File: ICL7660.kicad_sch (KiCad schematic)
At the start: 14 parts, among them J1 Vin, J2 GND, J3 Vout, J4 GND, J5 -Vout, U1 ICL7660

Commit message: 配置を修正
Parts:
- removed J4: GND, Connector_PinHeader_2.54mm:PinHeader_1x01_P2.54mm_Vertical, symbol Connector:Conn_01x01_Pin
- added H1, H2: MountingHole, MountingHole:MountingHole_3.2mm_M3, symbol Mechanical:MountingHole
- C1, C5: footprint Capacitor_THT:CP_Radial_D6.3mm_P2.50mm -> Capacitor_THT:CP_Radial_D10.0mm_P2.50mm
- R1, R2: footprint Resistor_THT:R_Axial_DIN0204_L3.6mm_D1.6mm_P7.62mm_Horizontal -> Resistor_THT:R_Axial_DIN0204_L3.6mm_D1.6mm_P2.54mm_Vertical
- renumbered J5 to J4
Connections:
- net GND: now also C5.1; no longer C5.2
- net at C6.1, J4.1 (Pin_1), R2.2: now also C5.2; no longer C5.1

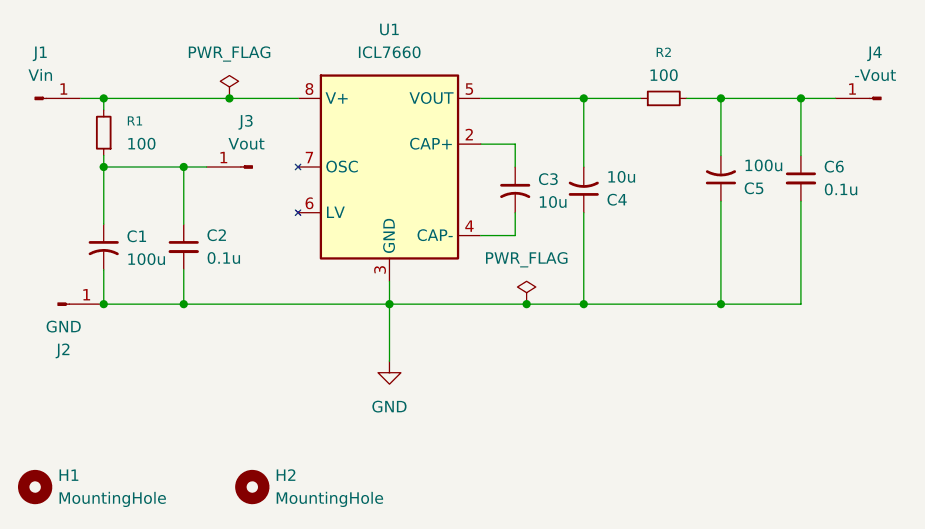
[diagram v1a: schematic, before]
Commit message: LED用の抵抗を追加
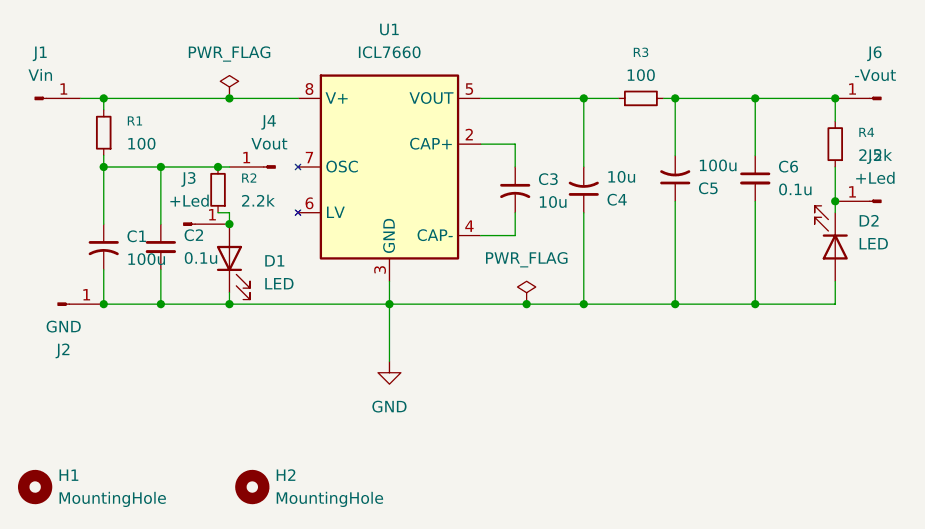
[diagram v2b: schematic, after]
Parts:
- added D1, D2: LED, symbol Device:LED
- added J3, J5: +Led, Connector_PinHeader_2.54mm:PinHeader_1x01_P2.54mm_Vertical, symbol Connector:Conn_01x01_Pin
- added R2, R4: 2.2k, Resistor_THT:R_Axial_DIN0204_L3.6mm_D1.6mm_P2.54mm_Vertical, symbol Device:R_Small
- renumbered J3 to J4, J4 to J6, R2 to R3
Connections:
- net GND: now also D1.1 (K), D2.2 (A)
- net at C1.1, C2.1, J4.1 (Pin_1)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: now also R2.2
- net at C5.2, C6.1, J6.1 (Pin_1)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: now also R4.2
- new net: D2.1 (K), J5.1 (Pin_1), R4.1
- new net: D1.2 (A), J3.1 (Pin_1), R2.1
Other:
- moved on the sheet: C2, C5, C6, J4, R3
